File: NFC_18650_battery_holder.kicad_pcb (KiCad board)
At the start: 2 copper layers, 70 x 78 mm, 9 parts, among them J1 Conn_01x06_Female, U1 ST25DV_8p, U2 MCQ4407

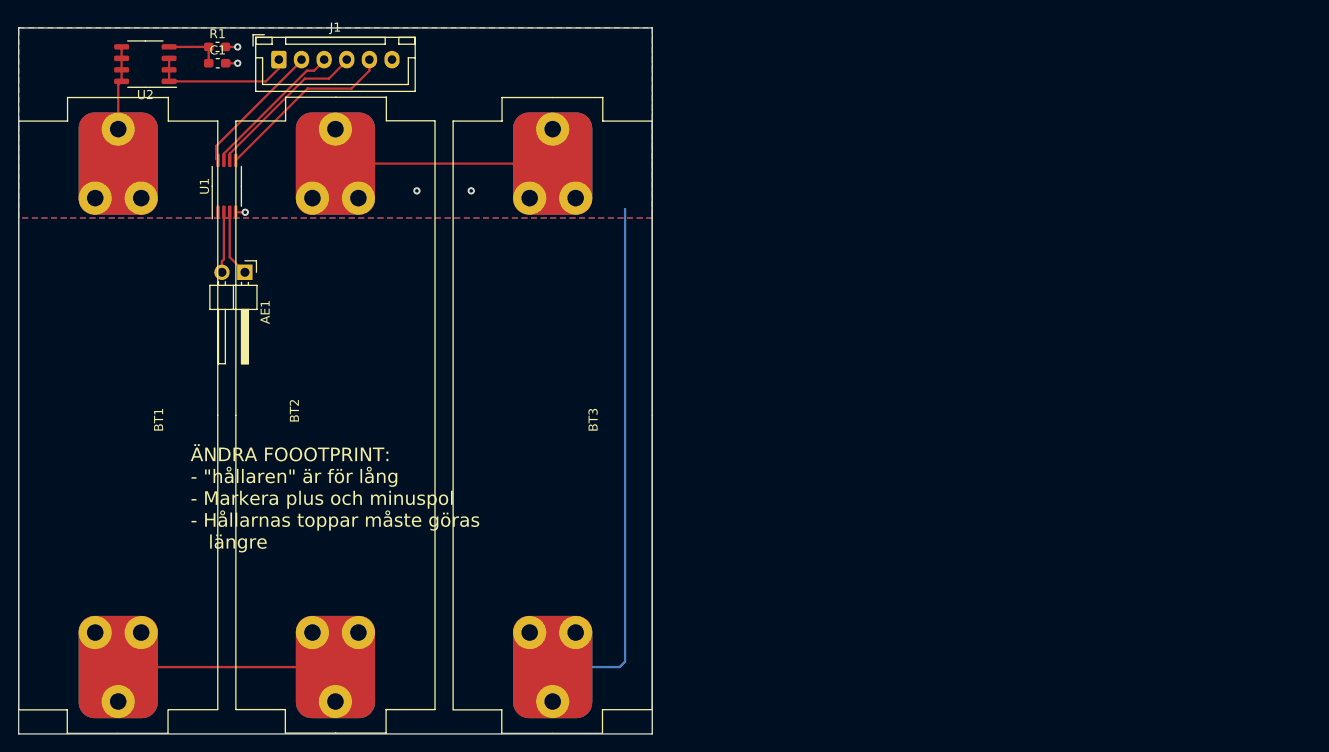
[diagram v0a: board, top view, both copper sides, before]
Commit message: 4.1uH antenna project done. Antenna was added to project via bitmap.
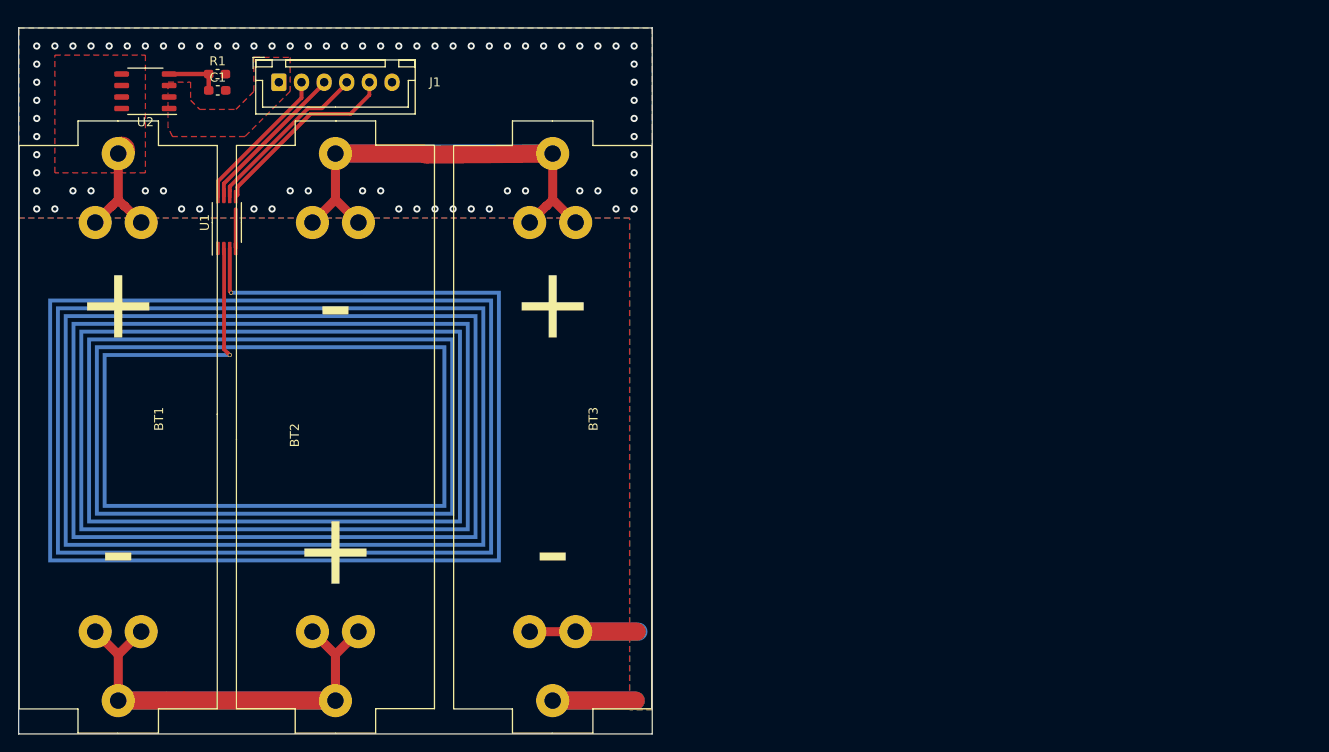
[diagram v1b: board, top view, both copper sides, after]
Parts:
- AE1: footprint Connector_PinHeader_2.54mm:PinHeader_1x02_P2.54mm_Horizontal -> NFC_18650_battery_holder:Antenna_4.1uH; moved to B.Cu
- BT1, BT2, BT3: footprint NFC_hatch_tmp:18650_holder_SMD -> NFC_hatch_tmp:18650_holder_SMD_65mm
- moved AE1 17.3 mm to (74.0, 97.0), turned to 180 degrees
- moved U1 4.00 mm to (69.0, 74.5)
- moved C1 3.00 mm to (68.0, 59.9)
- moved R1 3.00 mm to (68.0, 58.1)
- moved U2 3.00 mm to (60.0, 60.0)
- moved BT2 2.70 mm to (81.0, 98.5)
- moved J1 2.50 mm to (74.8, 59.0)
- moved BT1 0.10 mm to (57.0, 95.7)
- moved BT3 0.10 mm to (105.0, 95.7)
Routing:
- net Net-(BT1-Pad2): track 24.0 -> 72.5 mm
- net Net-(BT2-Pad2): track 24.0 -> 72.4 mm
- net /Sheet5FAF080E/BATT_RET: track 62.0 -> 41.7 mm, vias 5 -> 76
- net +BATT: track 16.2 -> 0.00 mm
- net Net-(AE1-Pad2): track 6.73 -> 12.0 mm
- net Net-(AE1-Pad1): track 7.33 -> 4.96 mm
- net Net-(J1-Pad2): track 15.1 -> 16.5 mm
- net Net-(J1-Pad5): track 20.1 -> 21.3 mm
- net Net-(J1-Pad3): track 16.2 -> 17.2 mm
- net Net-(J1-Pad4): track 18.0 -> 18.9 mm
- added copper zone on F.Cu, net +BATT
- added copper zone on F.Cu, net Net-(BT1-Pad1)
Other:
- board text added: "Antenna_4.1uH"
- board text removed: "ÄNDRA FOOOTPRINT: - "hållaren" är för lång - Markera plus och minuspol - Hållarnas toppar måste göras längre"

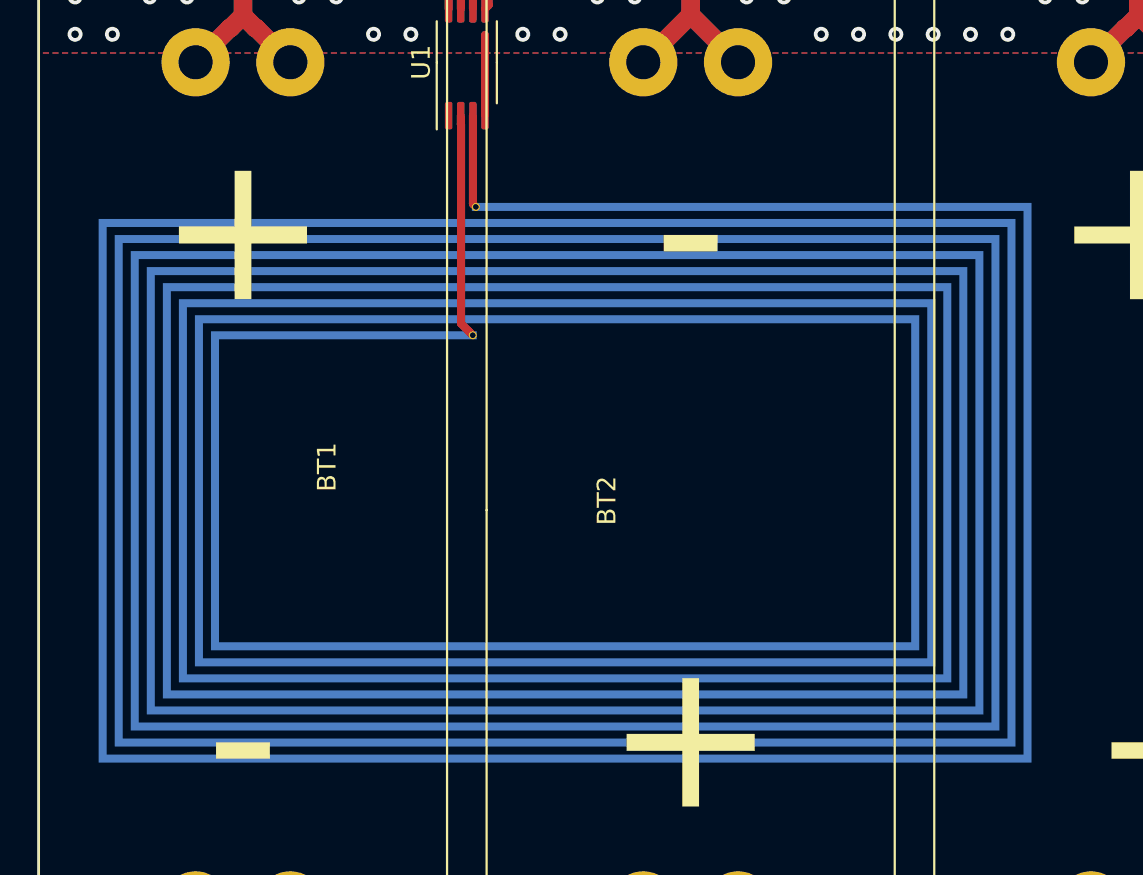
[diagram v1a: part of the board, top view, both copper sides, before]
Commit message: Antenna footprints done.
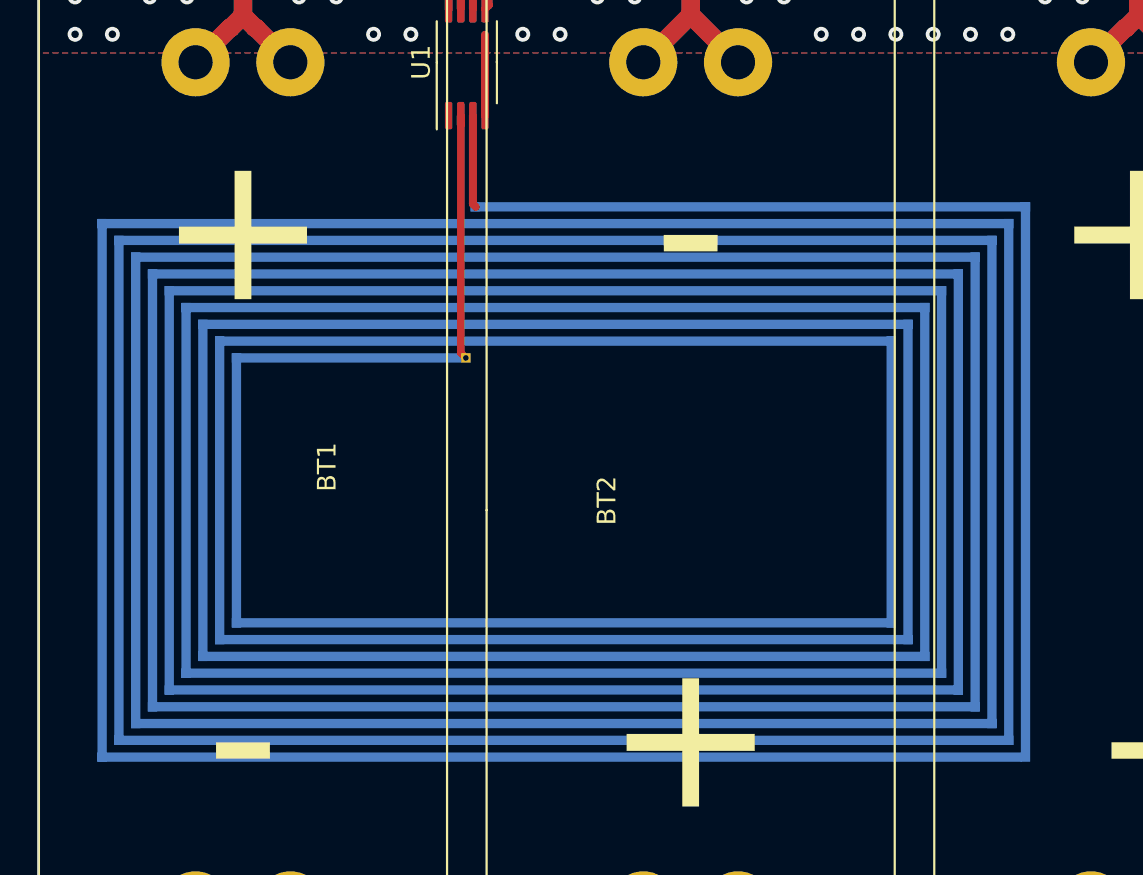
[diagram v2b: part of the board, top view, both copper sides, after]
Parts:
- AE1: footprint NFC_18650_battery_holder:Antenna_4.1uH -> NFC_18650_battery_holder:Antenna_4.58uH
- moved AE1 0.15 mm to (74.2, 97.0)
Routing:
- net Net-(AE1-Pad2): track 12.0 -> 13.6 mm
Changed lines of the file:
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@@
     (thickness 1.6)
     (drawings 5)
-    (tracks 145)
+    (tracks 144)
     (zones 0)
     (modules 9)
@@
   )
   (setup
-    (last_trace_width 0.43)
+    (last_trace_width 0.25)
     (user_trace_width 0.43)
     (user_trace_width 1)
@@
     (solder_mask_min_width 0.25)
     (aux_axis_origin 0 0)
-    (visible_elements FFFFFF7F)
+    (visible_elements 7FFFFFFF)
     (pcbplotparams
       (layerselection 0x010fc_ffffffff)
@@
     (add_net "Net-(J1-Pad4)")
     (add_net "Net-(J1-Pad5)")
-  )
-  (module NFC_18650_battery_holder:Antenna_4.1uH (layer B.Cu)
-    (at 74.05 97 180)
-    (fp_text reference AE1 (at -0.057 5.831) (layer B.SilkS) hide
-      (effects (font (size 1.524 1.524) (thickness 0.3)) (justify mirror))
-    )
-    (fp_text value Antenna_Loop (at 0.037 -6.591) (layer B.SilkS) hide
-      (effects (font (size 1.524 1.524) (thickness 0.3)) (justify mirror))
-    )
-    (fp_line (start 26 16) (end -26 16) (layer B.SilkS) (width 0.12))
-    (fp_line (start 26 -16) (end 26 16) (layer B.SilkS) (width 0.12))
-    (fp_line (start -26 -16) (end 26 -16) (layer B.SilkS) (width 0.12))
-    (fp_line (start -26 16) (end -26 -16) (layer B.SilkS) (width 0.12))
-    (fp_poly (pts (xy 4.781 14.531) (xy -10.00603 14.530205) (xy -24.793059 14.529411) (xy -24.793059 -14.614382)
-      (xy 24.355734 -14.614382) (xy 24.355734 13.668879) (xy -23.932527 13.668879) (xy -23.932527 -13.753849)
-      (xy 23.495202 -13.753849) (xy 23.495996 -0.471958) (xy 23.49679 12.809934) (xy -23.073582 12.809934)
-      (xy -23.073582 -12.894904) (xy 22.636257 -12.894904) (xy 22.636257 11.949401) (xy -22.213049 11.949401)
-      (xy -22.213049 -12.034372) (xy 21.775724 -12.034372) (xy 21.775724 11.088869) (xy -21.352517 11.088869)
-      (xy -21.352517 -11.173839) (xy 20.915192 -11.173839) (xy 20.915192 10.228336) (xy -20.491984 10.228336)
-      (xy -20.491984 -10.313307) (xy 20.054659 -10.313307) (xy 20.054659 9.367804) (xy -19.631452 9.367804)
-      (xy -19.631452 -9.452774) (xy 19.194127 -9.452774) (xy 19.194127 8.507271) (xy -18.770919 8.507271)
-      (xy -18.770919 -8.592241) (xy 18.333594 -8.592241) (xy 18.333594 7.649914) (xy 4.517442 7.649914)
-      (xy 4.517442 8.078592) (xy 18.765448 8.078592) (xy 18.765448 -9.024095) (xy -19.202773 -9.024095)
-      (xy -19.202773 8.939125) (xy 19.625981 8.939125) (xy 19.625981 -9.884628) (xy -20.063305 -9.884628)
-      (xy -20.063305 9.799658) (xy 0.21081 9.798864) (xy 20.484926 9.79807) (xy 20.484926 -10.743573)
-      (xy -20.92225 -10.743573) (xy -20.92225 10.658602) (xy 0.21081 10.659396) (xy 21.34387 10.660191)
-      (xy 21.34387 -11.605693) (xy -21.781195 -11.605693) (xy -21.781195 11.520723) (xy 22.204403 11.520723)
-      (xy 22.204403 -12.46305) (xy -22.641728 -12.46305) (xy -22.641728 12.37808) (xy 23.064936 12.37808)
-      (xy 23.064936 -13.323583) (xy -23.50226 -13.323583) (xy -23.50226 13.238612) (xy 23.925468 13.238612)
-      (xy 23.925468 -14.184115) (xy -24.362793 -14.184115) (xy -24.362793 14.099145) (xy 24.786001 14.099145)
-      (xy 24.786001 -15.044648) (xy -25.223325 -15.044648) (xy -25.223325 14.959677) (xy 4.781 14.959677)
-      (xy 4.781 14.531)) (layer B.Cu) (width 0))
-    (pad 1 thru_hole circle (at 4.567 14.746 180) (size 0.43 0.43) (drill 0.3) (layers *.Cu *.Mask)
+    (add_net "Net-(U1-Pad1)")
+  )
+  (module NFC_18650_battery_holder:Antenna_4.58uH (layer B.Cu)
+    (at 74.2 97 180)
+    (descr "A NFC antenna tuned for 13.56MHz")
+    (tags Antenna)
+    (fp_text reference AE1 (at 0 16) (layer B.SilkS)
+      (effects (font (size 1 1) (thickness 0.15)) (justify mirror))
+    )
+    (fp_text value Antenna_Loop (at 0 0) (layer B.Fab)
+      (effects (font (size 1 1) (thickness 0.15)) (justify mirror))
+    )
+    (fp_poly (pts (xy 5 15) (xy -25 15) (xy -25 14.5) (xy 5 14.5)) (layer B.Cu) (width 0))
+    (fp_poly (pts (xy 25 14.1) (xy -24.1 14.1) (xy -24.1 13.6) (xy 25 13.6)) (layer B.Cu) (width 0))
+    (fp_poly (pts (xy 24.1 13.2) (xy -23.2 13.2) (xy -23.2 12.7) (xy 24.1 12.7)) (layer B.Cu) (width 0))
+    (fp_poly (pts (xy 23.2 12.3) (xy -22.3 12.3) (xy -22.3 11.8) (xy 23.2 11.8)) (layer B.Cu) (width 0))
+    (fp_poly (pts (xy 22.3 11.4) (xy -21.4 11.4) (xy -21.4 10.9) (xy 22.3 10.9)) (layer B.Cu) (width 0))
+    (fp_poly (pts (xy 21.4 10.5) (xy -20.5 10.5) (xy -20.5 10) (xy 21.4 10)) (layer B.Cu) (width 0))
+    (fp_poly (pts (xy 20.5 9.6) (xy -19.6 9.6) (xy -19.6 9.1) (xy 20.5 9.1)) (layer B.Cu) (width 0))
+    (fp_poly (pts (xy 19.6 8.7) (xy -18.7 8.7) (xy -18.7 8.2) (xy 19.6 8.2)) (layer B.Cu) (width 0))
+    (fp_poly (pts (xy 18.7 7.8) (xy -17.8 7.8) (xy -17.8 7.3) (xy 18.7 7.3)) (layer B.Cu) (width 0))
+    (fp_poly (pts (xy 17.8 6.9) (xy 5 6.9) (xy 5 6.4) (xy 17.8 6.4)) (layer B.Cu) (width 0))
+    (fp_poly (pts (xy -25 15) (xy -25 -15) (xy -24.5 -15) (xy -24.5 15)) (layer B.Cu) (width 0))
+    (fp_poly (pts (xy -24.1 14.1) (xy -24.1 -14.1) (xy -23.6 -14.1) (xy -23.6 14.1)) (layer B.Cu) (width 0))
+    (fp_poly (pts (xy -23.2 13.2) (xy -23.2 -13.2) (xy -22.7 -13.2) (xy -22.7 13.2)) (layer B.Cu) (width 0))
+    (fp_poly (pts (xy -22.3 12.3) (xy -22.3 -12.3) (xy -21.8 -12.3) (xy -21.8 12.3)) (layer B.Cu) (width 0))
+    (fp_poly (pts (xy -21.4 11.4) (xy -21.4 -11.4) (xy -20.9 -11.4) (xy -20.9 11.4)) (layer B.Cu) (width 0))
+    (fp_poly (pts (xy -20.5 10.5) (xy -20.5 -10.5) (xy -20 -10.5) (xy -20 10.5)) (layer B.Cu) (width 0))
+    (fp_poly (pts (xy -19.6 9.6) (xy -19.6 -9.6) (xy -19.1 -9.6) (xy -19.1 9.6)) (layer B.Cu) (width 0))
+    (fp_poly (pts (xy -18.7 8.7) (xy -18.7 -8.7) (xy -18.2 -8.7) (xy -18.2 8.7)) (layer B.Cu) (width 0))
+    (fp_poly (pts (xy -17.8 7.8) (xy -17.8 -7.8) (xy -17.3 -7.8) (xy -17.3 7.8)) (layer B.Cu) (width 0))
+    (fp_poly (pts (xy 25 -15) (xy 25 14.1) (xy 24.5 14.1) (xy 24.5 -15)) (layer B.Cu) (width 0))
+    (fp_poly (pts (xy 24.1 -14.1) (xy 24.1 13.2) (xy 23.6 13.2) (xy 23.6 -14.1)) (layer B.Cu) (width 0))
+    (fp_poly (pts (xy 23.2 -13.2) (xy 23.2 12.3) (xy 22.7 12.3) (xy 22.7 -13.2)) (layer B.Cu) (width 0))
+    (fp_poly (pts (xy 22.3 -12.3) (xy 22.3 11.4) (xy 21.8 11.4) (xy 21.8 -12.3)) (layer B.Cu) (width 0))
+    (fp_poly (pts (xy 21.4 -11.4) (xy 21.4 10.5) (xy 20.9 10.5) (xy 20.9 -11.4)) (layer B.Cu) (width 0))
+    (fp_poly (pts (xy 20.5 -10.5) (xy 20.5 9.6) (xy 20 9.6) (xy 20 -10.5)) (layer B.Cu) (width 0))
+    (fp_poly (pts (xy 19.6 -9.6) (xy 19.6 8.7) (xy 19.1 8.7) (xy 19.1 -9.6)) (layer B.Cu) (width 0))
+    (fp_poly (pts (xy 18.7 -8.7) (xy 18.7 7.8) (xy 18.2 7.8) (xy 18.2 -8.7)) (layer B.Cu) (width 0))
+    (fp_poly (pts (xy 17.8 -7.8) (xy 17.8 6.9) (xy 17.3 6.9) (xy 17.3 -7.8)) (layer B.Cu) (width 0))
+    (fp_poly (pts (xy 25 -15) (xy -24.55 -15) (xy -24.55 -14.5) (xy 25 -14.5)) (layer B.Cu) (width 0))
+    (fp_poly (pts (xy 24.1 -14.1) (xy -24.1 -14.1) (xy -24.1 -13.6) (xy 24.1 -13.6)) (layer B.Cu) (width 0))
+    (fp_poly (pts (xy 23.2 -13.2) (xy -23.2 -13.2) (xy -23.2 -12.7) (xy 23.2 -12.7)) (layer B.Cu) (width 0))
+    (fp_poly (pts (xy 22.3 -12.3) (xy -22.3 -12.3) (xy -22.3 -11.8) (xy 22.3 -11.8)) (layer B.Cu) (width 0))
+    (fp_poly (pts (xy 21.4 -11.4) (xy -21.4 -11.4) (xy -21.4 -10.9) (xy 21.4 -10.9)) (layer B.Cu) (width 0))
+    (fp_poly (pts (xy 20.5 -10.5) (xy -20.5 -10.5) (xy -20.5 -10) (xy 20.5 -10)) (layer B.Cu) (width 0))
+    (fp_poly (pts (xy 19.6 -9.6) (xy -19.6 -9.6) (xy -19.6 -9.1) (xy 19.6 -9.1)) (layer B.Cu) (width 0))
+    (fp_poly (pts (xy 18.7 -8.7) (xy -18.7 -8.7) (xy -18.7 -8.2) (xy 18.7 -8.2)) (layer B.Cu) (width 0))
+    (fp_poly (pts (xy 17.8 -7.8) (xy -17.8 -7.8) (xy -17.8 -7.3) (xy 17.8 -7.3)) (layer B.Cu) (width 0))
+    (pad 2 thru_hole rect (at 5.25 6.65 180) (size 0.5 0.5) (drill 0.3) (layers *.Cu *.Mask)
+      (net 1 "Net-(AE1-Pad2)"))
+    (pad 1 smd rect (at 4.75 14.75 180) (size 0.5 0.5) (layers B.Cu B.Paste B.Mask)
       (net 2 "Net-(AE1-Pad1)"))
-    (pad 2 thru_hole circle (at 4.73 7.865 180) (size 0.43 0.43) (drill 0.3) (layers *.Cu *.Mask)
-      (net 1 "Net-(AE1-Pad2)"))
   )
   (module NFC_hatch_tmp:18650_holder_SMD_65mm (layer F.Cu)
@@
   (gr_line (start 46 131) (end 116 131) (layer Edge.Cuts) (width 0.05))
   (gr_line (start 46 53) (end 46 131) (layer Edge.Cuts) (width 0.05))
-  (segment (start 68.69499 88.50999) (end 69.105001 88.920001) (width 0.43) (layer F.Cu) (net 1))
-  (segment (start 69.105001 88.920001) (end 69.32 89.135) (width 0.43) (layer F.Cu) (net 1))
-  (segment (start 68.69499 77.84499) (end 68.69499 88.50999) (width 0.43) (layer F.Cu) (net 1))
   (segment (start 68.675 77.825) (end 68.69499 77.84499) (width 0.43) (layer F.Cu) (net 1))
   (segment (start 68.675 77.3625) (end 68.675 77.825) (width 0.43) (layer F.Cu) (net 1))
+  (segment (start 68.675 90.075) (end 68.95 90.35) (width 0.4) (layer F.Cu) (net 1))
+  (segment (start 68.675 77.3625) (end 68.675 90.075) (width 0.4) (layer F.Cu) (net 1))
   (segment (start 69.325 82.096) (end 69.483 82.254) (width 0.43) (layer F.Cu) (net 2))
   (segment (start 69.325 77.3625) (end 69.325 82.096) (width 0.43) (layer F.Cu) (net 2))

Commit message: 4.32uH Antenna board done!
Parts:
- AE1: value Antenna_Loop -> Antenna_4.32uH; footprint NFC_18650_battery_holder:Antenna_4.58uH -> NFC_18650_battery_holder:Antenna_4.32uH
- U1: footprint Package_SO:TSSOP-8_4.4x3mm_P0.65mm -> Package_SO:SOP-8_3.9x4.9mm_P1.27mm
- moved AE1 79.6 mm to (153.8, 96.4)
- moved U1 72.8 mm to (141.8, 73.5)
- moved BT1 72.8 mm to (129.8, 95.1)
- moved BT2 72.8 mm to (153.8, 97.9)
- moved BT3 72.8 mm to (177.8, 95.1)
- moved C1 72.8 mm to (140.8, 59.3)
- moved J1 72.8 mm to (147.5, 58.4)
- moved R1 72.8 mm to (140.7, 57.5)
- moved U2 72.8 mm to (132.8, 59.4)
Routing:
- net Net-(AE1-Pad2): track 13.6 -> 12.3 mm
- net /Sheet5FAF080E/BATT_RET: track 41.7 -> 40.5 mm, vias 76 -> 74
- net Net-(J1-Pad3): track 17.2 -> 18.2 mm
- net Net-(J1-Pad5): track 21.3 -> 20.6 mm
- net Net-(AE1-Pad1): track 4.96 -> 5.50 mm
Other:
- board text added: "B+"
- board text added: "B-"
- board text added: "GPO"
- board text added: "SCL"
- board text added: "SDA"
- board text added: "VCC_NFC"
- board text removed: "Antenna_4.1uH"

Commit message: 4.10uH Antenna created. Couryard was added to battery footprint and vias were removed around battery as a result.
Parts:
- AE1: value Antenna_4.32uH -> Antenna_4.10uH; footprint NFC_18650_battery_holder:Antenna_4.32uH -> NFC_18650_battery_holder:Antenna_4.10uH
- moved J1 1.58 mm to (146.8, 57.0)
- moved C1 0.86 mm to (140.0, 58.9)
- moved U2 0.86 mm to (132.0, 59.0)
- moved AE1 0.86 mm to (153.0, 96.0)
- moved BT1 0.86 mm to (129.0, 94.7)
- moved BT2 0.86 mm to (153.0, 97.5)
- moved BT3 0.86 mm to (177.0, 94.7)
- moved R1 0.86 mm to (140.0, 57.1)
- moved U1 0.86 mm to (141.0, 73.1)
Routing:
- net Net-(J1-Pad2): track 16.6 -> 17.6 mm
- net Net-(J1-Pad5): track 20.6 -> 21.6 mm
- net Net-(J1-Pad4): track 19.3 -> 20.3 mm
- net Net-(J1-Pad3): track 18.2 -> 19.2 mm
- net /Sheet5FAF080E/BATT_RET: vias 74 -> 62
